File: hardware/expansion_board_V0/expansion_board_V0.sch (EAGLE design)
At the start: 225 parts, among them CON2 NC, IC1 DRV8402, IC5 DRV8402, IC6 DRV8402, IC7 DRV8402, Q2 25MHz, U1 AM26C32, U2 AM26C32, U4 LAN9514

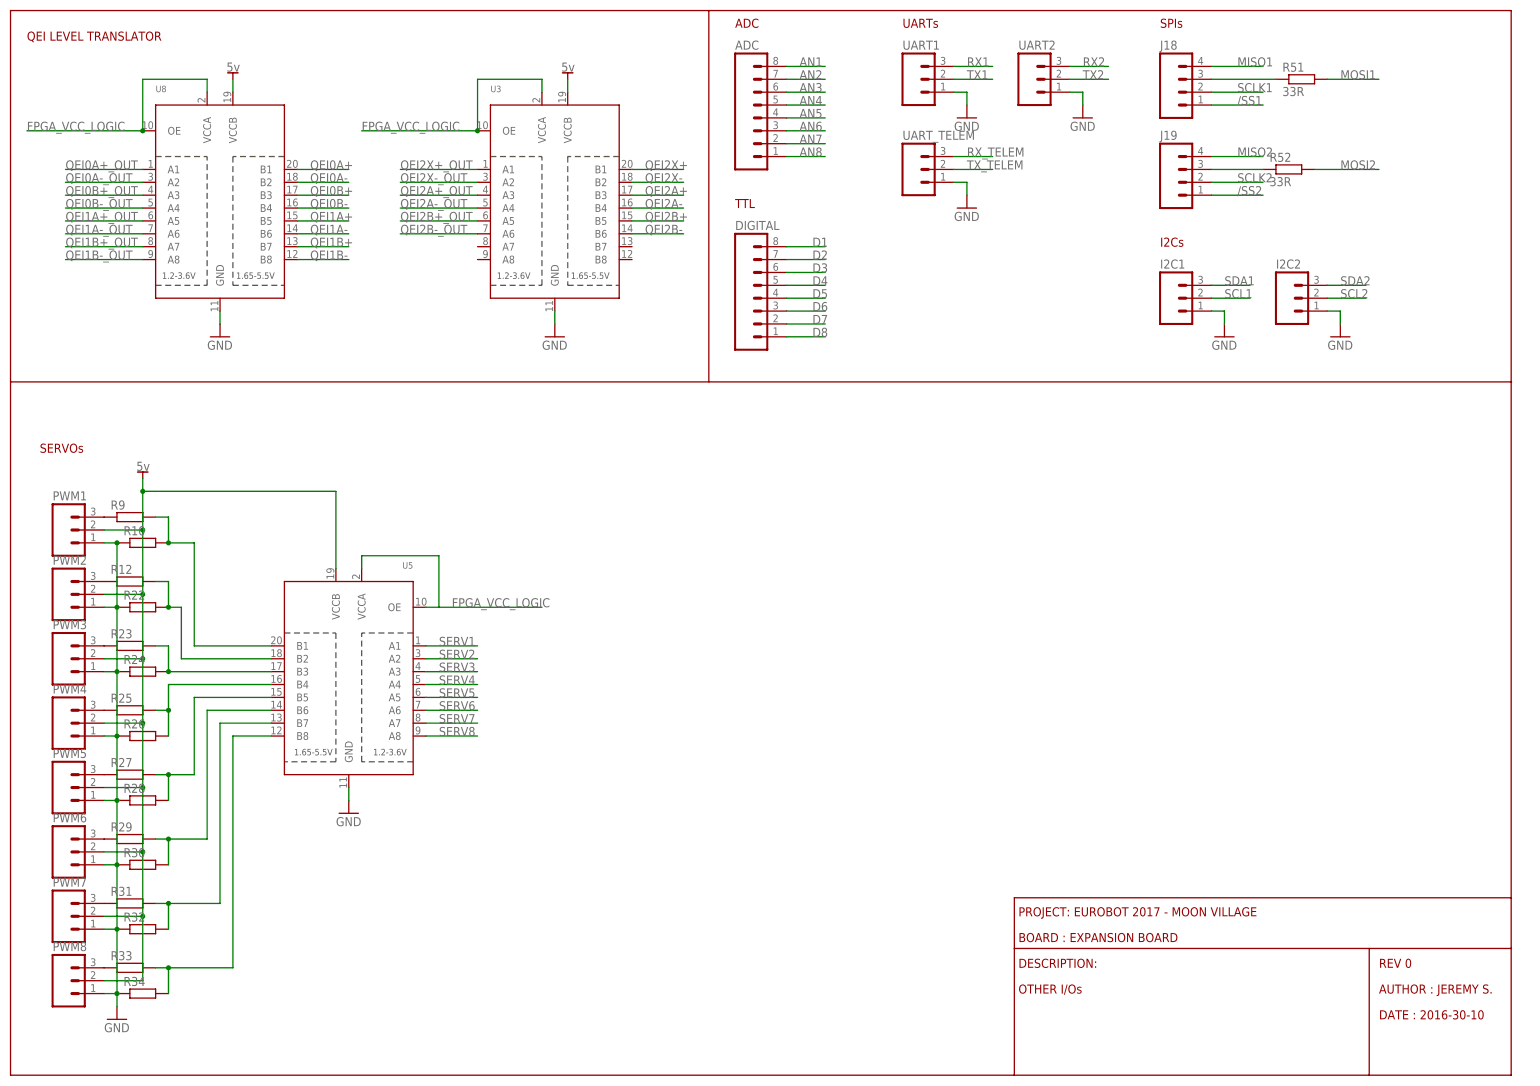
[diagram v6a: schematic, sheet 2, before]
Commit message: Add current sense for motor and servo
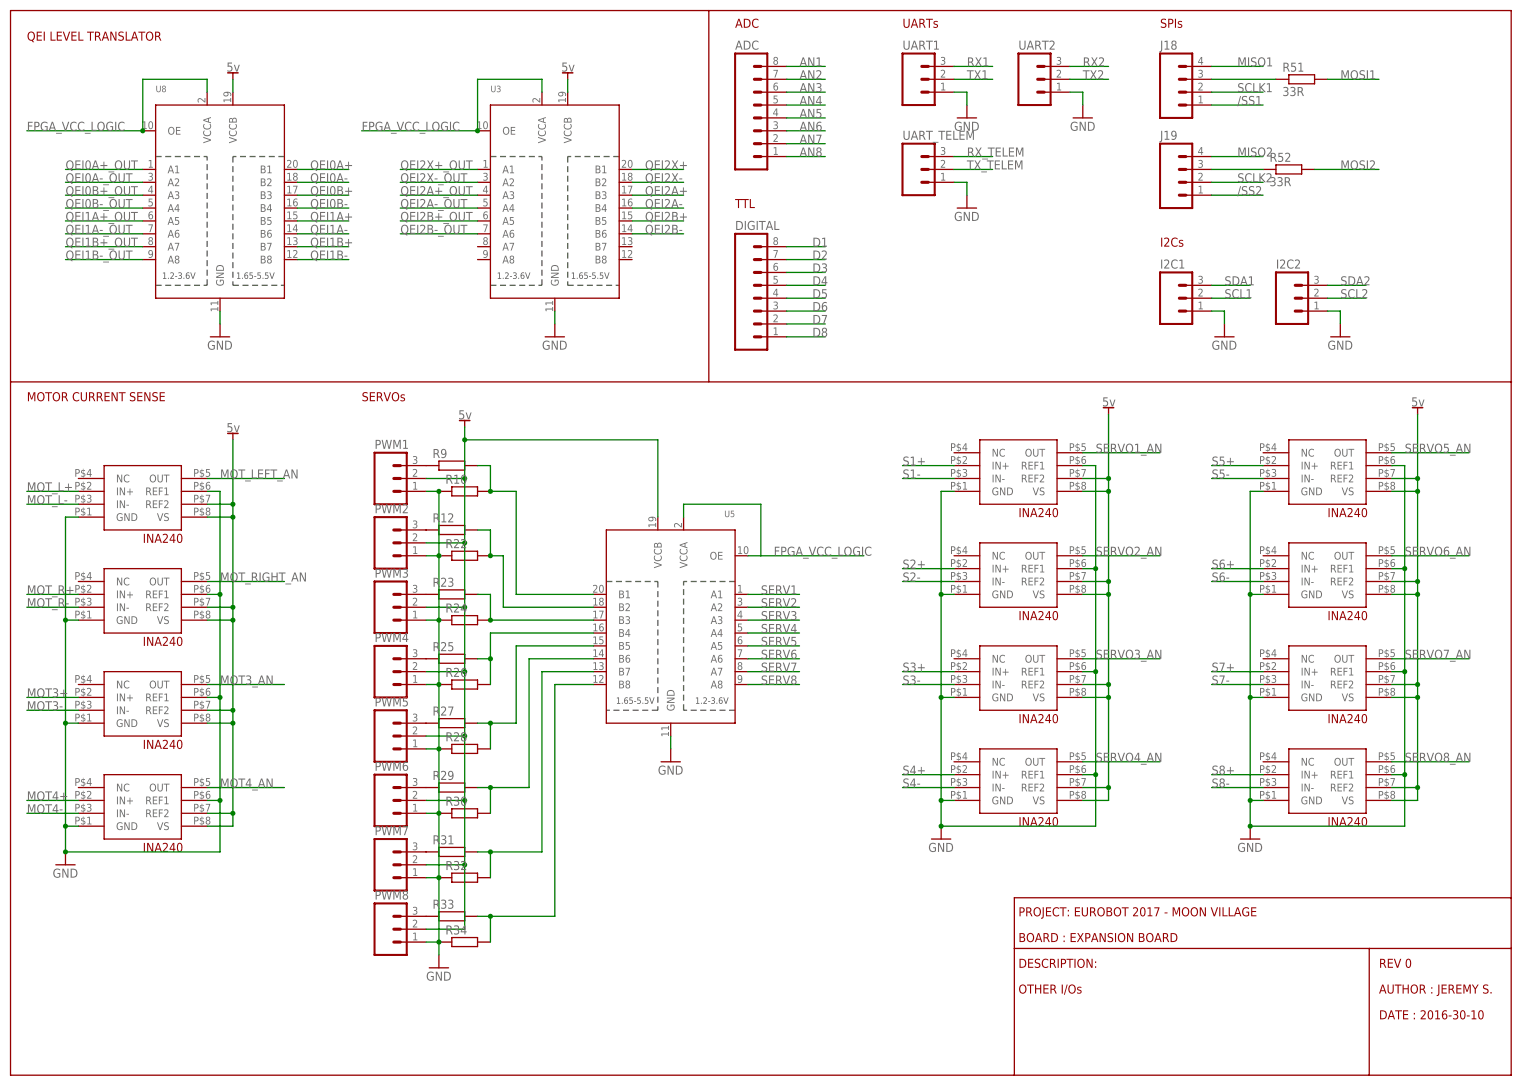
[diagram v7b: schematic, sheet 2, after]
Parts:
- added U$1, U$10, U$14, U$15, U$17, U$2, U$4, U$5, U$6, U$7, U$8, U$9: INA240-TSSOP, Texas Instruments_By_element14_Batch_1:INA240-TSSOP
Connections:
- new net MOT3+: U$4.IN+
- new net MOT3-: U$4.IN-
- new net MOT3_AN: U$4.OUT
- new net MOT4+: U$5.IN+
- new net MOT4-: U$5.IN-
- new net MOT4_AN: U$5.OUT
- new net MOT_L+: U$1.IN+
- new net MOT_L-: U$1.IN-
- new net MOT_LEFT_AN: U$1.OUT
- new net MOT_R+: U$2.IN+
- new net MOT_R-: U$2.IN-
- new net MOT_RIGHT_AN: U$2.OUT
- new net S1+: U$6.IN+
- new net S1-: U$6.IN-
- new net S2+: U$7.IN+
- new net S2-: U$7.IN-
- new net S3+: U$8.IN+
- new net S3-: U$8.IN-
- new net S4+: U$9.IN+
- new net S4-: U$9.IN-
- new net S5+: U$10.IN+
- new net S5-: U$10.IN-
- new net S6+: U$14.IN+
- new net S6-: U$14.IN-
- new net S7+: U$15.IN+
- new net S7-: U$15.IN-
- new net S8+: U$17.IN+
- new net S8-: U$17.IN-
- new net SERVO1_AN: U$6.OUT
- new net SERVO2_AN: U$7.OUT
- new net SERVO3_AN: U$8.OUT
- new net SERVO4_AN: U$9.OUT
- new net SERVO5_AN: U$10.OUT
- new net SERVO6_AN: U$14.OUT
- new net SERVO7_AN: U$15.OUT
- new net SERVO8_AN: U$17.OUT
- net 5V: now also U$1.REF2, U$1.VS, U$10.REF2, U$10.VS, U$14.REF2, U$14.VS, U$15.REF2, U$15.VS, U$17.REF2, U$17.VS, U$2.REF2, U$2.VS, U$4.REF2, U$4.VS, U$5.REF2, U$5.VS, U$6.REF2, U$6.VS, U$7.REF2, U$7.VS, U$8.REF2, U$8.VS, U$9.REF2, U$9.VS
- net GND: now also U$1.GND, U$1.REF1, U$10.GND, U$10.REF1, U$14.GND, U$14.REF1, U$15.GND, U$15.REF1, U$17.GND, U$17.REF1, U$2.GND, U$2.REF1, U$4.GND, U$4.REF1, U$5.GND, U$5.REF1, U$6.GND, U$6.REF1, U$7.GND, U$7.REF1, U$8.GND, U$8.REF1, U$9.GND, U$9.REF1
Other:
- note added: "MOTOR CURRENT SENSE"
- moved on the sheet: PWM1, PWM2, PWM3, PWM4, PWM5, PWM6, PWM7, PWM8, R10, R12, R22, R23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

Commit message: -
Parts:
- added C100, C101, C102, C104, C105, C106, C107, C113, C114, C115, C116, C117, C122, C123, C129, C130, C131, C132, C48, C49, C50, C51, C75, C76, C77, C78, C83, C84, C85, C88, C98, C99: 100n, iocene:C_603
- added C103, C121, C135, C144, C81: 10n, iocene:C_402
- added C108, C109, C110, C111, C124, C125, C126, C127, C52, C53, C54, C55, C93, C94, C95, C96: 1µ, iocene:C_603
- added C112, C120, C128, C134, C137, C138, C139, C140, C143, C145, C147, C189, C190, C191, C192, C193, C194, C195, C20, C205, C22, C27, C56, C79, C82, C97: 100n, iocene:C_402
- added C118, C119, C133, C136, C196, C197, C198, C199, C200, C201, C202, C203, C204, C80: 1n, iocene:C_402
- added C141: 10u, iocene:C_805
- added C142: 1u, iocene:C_603
- added C146: 100p, iocene:C_402
- added C188, C206, C207: 22n, iocene:C_402
- added C21: 100n, iocene:C_805
- added CON1: M4, iocene:CON2_3.81
- added CON10: QEI3, iocene:CON6_2.54S
- added CON11: QEI4, iocene:CON6_2.54S
- added CON12, CON13, CON14, CON15, CON16, CON17, CON18, CON19: S1, iocene:CON3_2.54S
- added CON3: M5, iocene:CON2_3.81
- added CON4: M3, iocene:CON2_3.81
- added CON5: M6, iocene:CON2_3.81
- added CON6: M2, iocene:CON2_3.81
- added CON7: M1, iocene:CON2_3.81
- added CON8: QEI1, iocene:CON5_2.54S
- added CON9: QEI2, iocene:CON5_2.54S
- added D1: SMP12A, iocene:ZENER
- added IC3: REF5030I, IMU:REF5025I
- added J1, J11, J12, J13, J14, J15, J16, J17, J2, J3, J4, J5, J6: 0, iocene:JUMP_402
- added J10, J8: 0, iocene:JUMP_603
- added J7, J9: nc, iocene:JUMP_603
- added L10, L11, L12, L2, L3, L4, L7, L9: SRN2512-R24M, iocene:INDUCTANCE_2520
- added R102, R103, R82, R83, R84, R85, R86, R87, R88, R89: 1k, iocene:R_402
- added R35, R50, R56, R58, R64, R76, R78, R80: 0.01, iocene:R_603
- added R36, R40, R41, R42: 30k, iocene:R_402
- added R37, R38, R43, R44: ULR15S-R0055FT2, iocene:R_ULR15S-R0055FT2
- added R39, R45, R46, R47, R48, R53, R57, R59, R60, R75, R77, R79, R81: 10k, iocene:R_402
- added R49: 1M, iocene:R_402
- added U$19: MB85RS64PNF, iocene:MEM_SPI_SOIC
- added U$20, U$23, U$24, U$25: DRV8432, iocene:DRV84X2_DRV8432
- added U$21, U$22, U$26, U$27: INA240-A2, Texas Instruments_By_element14_Batch_1:INA240-TSSOP
- added U6, U7: (no value), adafruit:TXB0108PWR
- added U9: OPA376, iocene:OPA376
- added UW1: ADS1258, IMU:ADS1258
- added UW2: 32.768kHz, IMU:QUARTZ_1206
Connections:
- new net 12V: C108.P$2, C109.P$2, C110.P$2, C111.P$2, C124.P$2, C125.P$2, C126.P$2, C127.P$2, C52.P$2, C53.P$2, C54.P$2, C55.P$2, C93.P$2, C94.P$2, C95.P$2, C96.P$2, J10.1, J8.1, U$20.VDD, U$23.VDD, U$24.VDD, U$25.VDD
- new net 24V: C114.P$2, C115.P$2, C116.P$2, C117.P$2, C129.P$2, C130.P$2, C131.P$2, C132.P$2, J7.1, J9.1, U$24.VDDA, U$24.VDDB, U$24.VDDC, U$24.VDDD, U$25.VDDA, U$25.VDDB, U$25.VDDC, U$25.VDDD
- new net A5V: CON12.3, CON13.3, CON14.3, CON15.3, CON16.3, CON17.3, CON18.3, CON19.3
- new net ADC_VREF: C103.P$2, C121.P$2, C135.P$2, C81.P$2, U$21.REF1, U$22.REF1, U$26.REF1, U$27.REF1
- new net ADS1_CS: UW1.CS
- new net ADS1_M: R48.P$1, UW1.MUXOUTP
- new net ADS1_P: C146.P$2, R49.P$2, U9.OUT, UW1.ADCINP
- new net ADS1_RDY: UW1.DRDY
- new net ADS1_V: C141.P$1, C144.P$2, J17.2, UW1.VREFP
- new net ADS_MISO: UW1.DOUT
- new net ADS_MOSI: UW1.DIN
- new net ADS_RST: UW1.RESET
- new net ADS_SCLK: UW1.SCLK
- new net AN0: UW1.AIN0
- new net AN10: UW1.AIN10
- new net AN11: UW1.AIN11
- new net AN12: UW1.AIN12
- new net AN13: UW1.AIN13
- new net AN14: UW1.AIN14
- new net AN15: UW1.AIN15
- new net AN9: UW1.AIN9
- new net M1_CS: C133.P$2, R46.P$2
- new net M2_CS: C119.P$2, R45.P$2
- new net M34_FAULT: U$20.FAULT, U$20.OT
- new net M3_CS: C118.P$2, R59.P$2
- new net M3_PWMA: U$20.PWMA
- new net M3_PWMB: U$20.PWMB
- new net M4_CS: C80.P$2, R39.P$2
- new net M56_FAULT: U$23.FAULT, U$23.OT
- new net M5_PWMA: U$23.PWMA
- new net M5_PWMB: U$23.PWMB
- new net M6_PWMA: U$23.PWMC
- new net M6_PWMB: U$23.PWMD
- new net MEM_CS: U$19.CS
- new net MISO: U$19.SDO
- new net MOSI: U$19.SDI
- new net N$10: C50.P$1, U$20.BSTC
- new net N$100: C107.P$1, U$24.BSTD
- new net N$101: C106.P$1, U$24.BSTC
- new net N$102: C104.P$1, U$24.BSTB
- new net N$103: C102.P$2, L2.2, U$24.OUTA
- new net N$104: C104.P$2, L4.2, U$24.OUTB
- new net N$105: C106.P$2, L3.2, U$24.OUTC
- new net N$106: C107.P$2, L7.2, U$24.OUTD
- new net N$114: C112.P$2, J11.1, J12.1, U$24.VCAP
- new net N$115: R41.P$1, U$24.OC_ADJ
- new net N$116: C105.P$1, U$25.BSTA
- new net N$117: J11.2, U$24.RST_AB, U$24.RST_CD
- new net N$118: J13.2, U$24.M1
- new net N$119: J12.2, U$24.M2
- new net N$12: C49.P$1, U$20.BSTB
- new net N$120: C123.P$1, U$25.BSTD
- new net N$121: R45.P$1, U$26.OUT
- new net N$122: CON6.1, R44.P$2, U$26.IN-
- new net N$123: C122.P$1, U$25.BSTC
- new net N$124: L3.1, L7.1, R44.P$1, U$26.IN+
- new net N$125: C113.P$1, U$25.BSTB
- new net N$126: CON6.2, L2.1, L4.1
- new net N$127: C105.P$2, L9.2, U$25.OUTA
- new net N$128: C113.P$2, L11.2, U$25.OUTB
- new net N$129: C122.P$2, L10.2, U$25.OUTC
- new net N$130: C123.P$2, L12.2, U$25.OUTD
- new net N$131: C128.P$2, J14.1, J15.1, U$25.VCAP
- new net N$132: R42.P$1, U$25.OC_ADJ
- new net N$133: J14.2, U$25.RST_AB, U$25.RST_CD
- new net N$134: J16.2, U$25.M1
- new net N$135: J15.2, U$25.M2
- new net N$136: R46.P$1, U$27.OUT
- new net N$137: CON7.1, R43.P$2, U$27.IN-
- new net N$138: L10.1, L12.1, R43.P$1, U$27.IN+
- new net N$139: CON7.2, L11.1, L9.1
- new net N$14: C48.P$2, R37.P$1, U$20.OUTA, U$21.IN-
- new net N$140: C136.P$2, CON8.3, R88.P$1, U6.B1
- new net N$141: C203.P$2, CON9.2, R103.P$1, U6.B8
- new net N$142: C204.P$2, CON9.3, R102.P$1, U6.B7
- new net N$143: C197.P$2, CON10.4, R83.P$1, U7.B2
- new net N$144: C196.P$2, CON10.3, R82.P$1, U7.B1
- new net N$145: C199.P$2, CON11.5, R87.P$1, U7.B8
- new net N$146: C200.P$2, CON11.4, R86.P$1, U7.B7
- new net N$147: C201.P$2, CON11.3, R85.P$1, U7.B6
- new net N$148: C198.P$2, CON10.5, R84.P$1, U7.B3
- new net N$149: CON12.1, R35.P$1, R47.P$2
- new net N$150: R48.P$2, R49.P$1, U9.+
- new net N$151: C188.P$2, UW1.PLLCAP
- new net N$152: C206.P$2, UW1.XTAL1, UW2.P1
- new net N$153: C207.P$2, UW1.XTAL2, UW2.P2
- new net N$156: CON13.1, R50.P$1, R53.P$2
- new net N$157: CON14.1, R56.P$1, R57.P$2
- new net N$158: CON15.1, R58.P$1, R60.P$2
- new net N$159: CON16.1, R64.P$1, R75.P$2
- new net N$16: C49.P$2, CON4.1, U$20.OUTB
- new net N$160: CON17.1, R76.P$1, R77.P$2
- new net N$161: CON18.1, R78.P$1, R79.P$2
- new net N$162: CON19.1, R80.P$1, R81.P$2
- new net N$170: C142.P$1, IC3.TRIM
- new net N$171: IC3.VOUT, J17.1
- new net N$18: J3.2, U$20.M1
- new net N$2: C202.P$2, CON8.2, R89.P$1, U6.B2
- new net N$46: J2.2, U$20.M2
- new net N$5: J1.2, U$20.RST_AB, U$20.RST_CD
- new net N$55: C50.P$2, CON1.2, U$20.OUTC
- new net N$56: C51.P$2, R38.P$1, U$20.OUTD, U$22.IN+
- new net N$57: C56.P$2, J1.1, U$20.VCAP
- new net N$60: CON4.2, R37.P$2, U$21.IN+
- new net N$62: R36.P$1, U$20.OC_ADJ
- new net N$65: R59.P$1, U$21.OUT
- new net N$7: C48.P$1, U$20.BSTA
- new net N$76: CON1.1, R38.P$2, U$22.IN-
- new net N$77: C83.P$1, U$23.BSTA
- new net N$78: C88.P$1, U$23.BSTD
- new net N$79: C85.P$1, U$23.BSTC
- new net N$8: C51.P$1, U$20.BSTD
- new net N$80: C84.P$1, U$23.BSTB
- new net N$81: C83.P$2, CON3.2, U$23.OUTA
- new net N$82: C84.P$2, CON3.1, U$23.OUTB
- new net N$83: C85.P$2, CON5.2, U$23.OUTC
- new net N$84: C88.P$2, CON5.1, U$23.OUTD
- new net N$85: C97.P$2, J4.1, U$23.VCAP
- new net N$86: R40.P$1, U$23.OC_ADJ
- new net N$87: C75.P$2, C76.P$2, C77.P$2, C78.P$2, J7.2, J8.2, U$20.VDDA, U$20.VDDB, U$20.VDDC, U$20.VDDD
- new net N$88: J4.2, U$23.RST_AB, U$23.RST_CD
- new net N$89: R39.P$1, U$22.OUT
- new net N$90: J6.2, U$23.M1
- new net N$91: J5.2, U$23.M2
- new net N$92: C100.P$2, C101.P$2, C98.P$2, C99.P$2, J10.2, J9.2, U$23.VDDA, U$23.VDDB, U$23.VDDC, U$23.VDDD
- new net N$99: C102.P$1, U$24.BSTA
- new net QEI1_A: U6.A1
- new net QEI1_B: U6.A2
- new net QEI2_A: U6.A7
- new net QEI2_B: U6.A8
- new net QEI3_A: U7.A1
- new net QEI3_B: U7.A2
- new net QEI3_Z: U7.A3
- new net QEI4_A: U7.A6
- new net QEI4_B: U7.A7
- new net QEI4_Z: U7.A8
- new net S1°: CON12.2, CON13.2, CON14.2, CON15.2, CON16.2, CON17.2, CON18.2, CON19.2
- new net SCLK: U$19.SCK
- net 3V3: now also C137.P$2, C20.P$2, C21.P$1, U$19.HOLD, U$19.VDD, U$19.WP, U6.OE, U6.VCCA, U7.OE, U7.VCCA, UW1.DVDD, UW1.PWDN, UW1.START
- net 5V: now also C120.P$2, C134.P$2, C138.P$2, C139.P$2, C140.P$2, C143.P$2, C147.P$2, C205.P$2, C22.P$2, C27.P$2, C79.P$2, C82.P$2, CON10.1, CON11.1, CON8.5, CON9.5, IC3.VIN, R102.P$2, R103.P$2, R82.P$2, R83.P$2, R84.P$2, R85.P$2, R86.P$2, R87.P$2, R88.P$2, R89.P$2, U$21.VS, U$22.VS, U$26.VS, U$27.VS, U6.VCCB, U7.VCCB, U9.VCC, UW1.AVDD
- net AN1: now also UW1.AIN1
- net AN2: now also UW1.AIN2
- net AN3: now also UW1.AIN3
- net AN4: now also UW1.AIN4
- net AN5: now also UW1.AIN5
- net AN6: now also UW1.AIN6
- net AN7: now also UW1.AIN7
- net AN8: now also C145.P$2, C189.P$2, C190.P$2, C191.P$2, C192.P$2, C193.P$2, C194.P$2, C195.P$2, R47.P$1, R53.P$1, R57.P$1, R60.P$1, R75.P$1, R77.P$1, R79.P$1, R81.P$1, UW1.AIN8
- net GND: now also C100.P$1, C101.P$1, C103.P$1, C108.P$1, C109.P$1, C110.P$1, C111.P$1, C112.P$1, C114.P$1, C115.P$1, C116.P$1, C117.P$1, C118.P$1, C119.P$1, C120.P$1, C121.P$1, C124.P$1, C125.P$1, C126.P$1, C127.P$1, C128.P$1, C129.P$1, C130.P$1, C131.P$1, C132.P$1, C133.P$1, C134.P$1, C135.P$1, C136.P$1, C137.P$1, C138.P$1, C139.P$1, C140.P$1, C141.P$2, C142.P$2, C143.P$1, C144.P$1, C145.P$1, C146.P$1, C147.P$1, C188.P$1, C189.P$1, C190.P$1, C191.P$1, C192.P$1, C193.P$1, C194.P$1, C195.P$1, C196.P$1, C197.P$1, C198.P$1, C199.P$1, C20.P$1, C200.P$1, C201.P$1, C202.P$1, C203.P$1, C204.P$1, C205.P$1, C206.P$1, C207.P$1, C21.P$2, C22.P$1, C27.P$1, C52.P$1, C53.P$1, C54.P$1, C55.P$1, C56.P$1, C75.P$1, C76.P$1, C77.P$1, C78.P$1, C79.P$1, C80.P$1, C81.P$1, C82.P$1, C93.P$1, C94.P$1, C95.P$1, C96.P$1, C97.P$1, C98.P$1, C99.P$1, CON10.2, CON10.6, CON11.2, CON11.6, CON8.1, CON8.4, CON9.1, CON9.4, IC3.GND, IC3.NC, J13.1, J16.1, J2.1, J3.1, J5.1, J6.1, R35.P$2, R36.P$2, R40.P$2, R41.P$2, R42.P$2, R50.P$2, R56.P$2, R58.P$2, R64.P$2, R76.P$2, R78.P$2, R80.P$2, U$19.GND, U$20.GND, U$20.GNDA, U$20.GNDB, U$20.GNDC, U$20.GNDD, U$20.M3, U$21.GND, U$21.NC, U$21.REF2, U$22.GND, U$22.NC, U$22.REF2, U$23.GND, U$23.GNDA, U$23.GNDB, U$23.GNDC, U$23.GNDD, U$23.M3, U$24.GND, U$24.GNDA, U$24.GNDB, U$24.GNDC, U$24.GNDD, U$24.M3, U$24.PWMC, U$24.PWMD, U$25.GND, U$25.GNDA, U$25.GNDB, U$25.GNDC, U$25.GNDD, U$25.M3, U$25.PWMC, U$25.PWMD, U$26.GND, U$26.NC, U$26.REF2, U$27.GND, U$27.NC, U$27.REF2, U6.GND, U7.GND, U9.-, U9.GND, UW1.ADCINN, UW1.AINCOM, UW1.AVSS, UW1.CLKSEL, UW1.DGND, UW1.VREFN
- net M1_FAULT: now also U$25.FAULT, U$25.OT
- net M1_PWMA: now also U$25.PWMA
- net M1_PWMB: now also U$25.PWMB
- net M2_FAULT: now also U$24.FAULT, U$24.OT
- net M2_PWMA: now also U$24.PWMA
- net M2_PWMB: now also U$24.PWMB
- net M4_PWMA: now also U$20.PWMC
- net M4_PWMB: now also U$20.PWMD
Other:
- note added: "A2"
- note added: "Ajouter des isolateurs ?"
- note added: "Ajouter du 5v et une masse à chaque connecteur"
- note added: "Ajouter les pullup I2C + pin IO (reset)"
- note added: "Ajouter pont diviseur + filtre RC pour AN"
- note added: "Comme on a des codeurs low cost, on n'a pas le différentiel"
- note added: "FPGA logic"
- note added: "HV motors"
- note added: "Motors"
- note added: "Sensors"
- note added: "Servos"
- note added: "TXB0108"
- note added: "en DQS c'est plus facile à souder"
- note added: "pin 1 et 4 inversées"
